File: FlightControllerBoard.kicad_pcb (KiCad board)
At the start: 2 copper layers, 50 x 60 mm, 88 parts, among them J1 Conn_01x02, J10 Conn_01x03_Male, J11 USB_C_Receptacle_USB2.0, J12 Conn_02x03_Odd_Even, J2 Conn_01x03_Male, J3 Conn_01x03_Male, J4 Conn_01x03_Male, J5 Conn_01x03_Male, J6 Conn_01x03_Male, J7 Conn_01x03_Male, J8 Conn_01x03_Male, J9 Conn_01x03_Male, Q1 BSS138, SW1 SW_Push, U1 FT230XQ, U2 LMZM23600, U3 ATmega2560-16AU, U4 BNO055, Y1 16MHz, Y2 32.768kHz

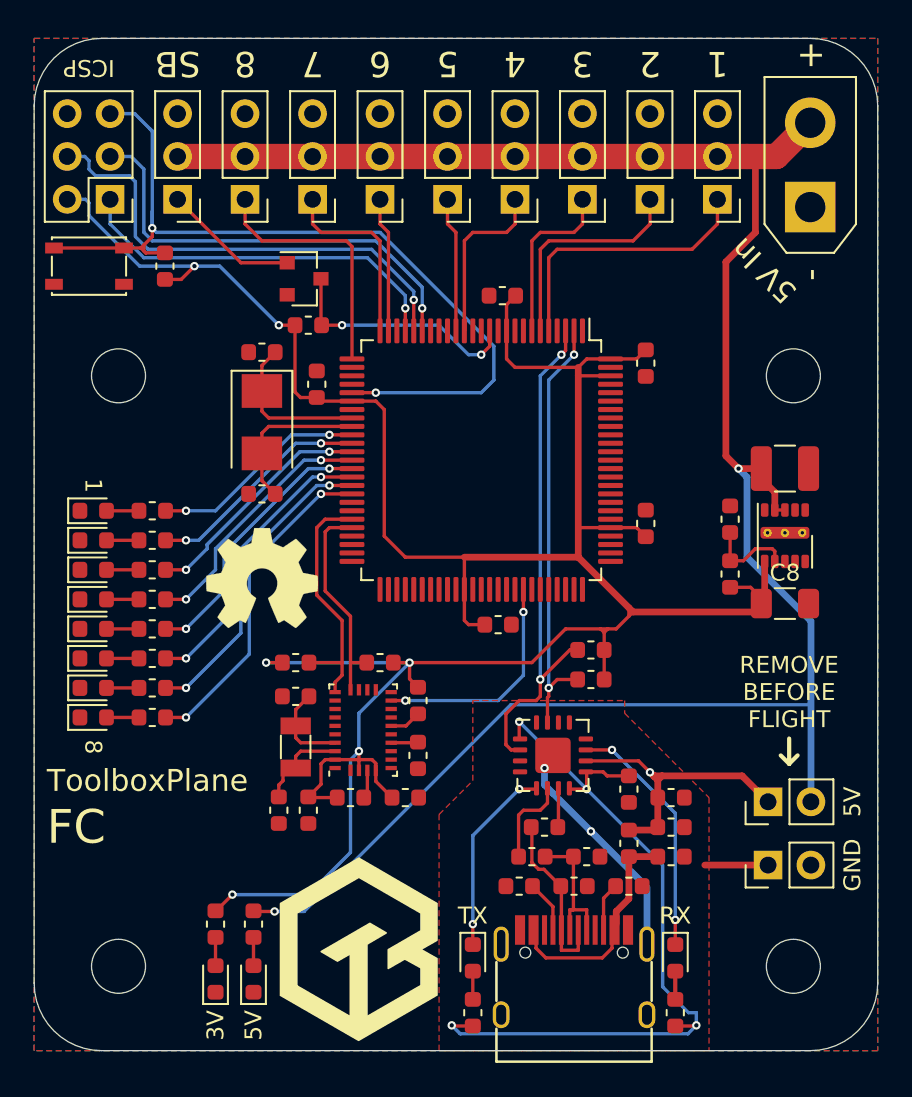
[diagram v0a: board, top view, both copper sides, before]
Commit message: optimize gnd connections
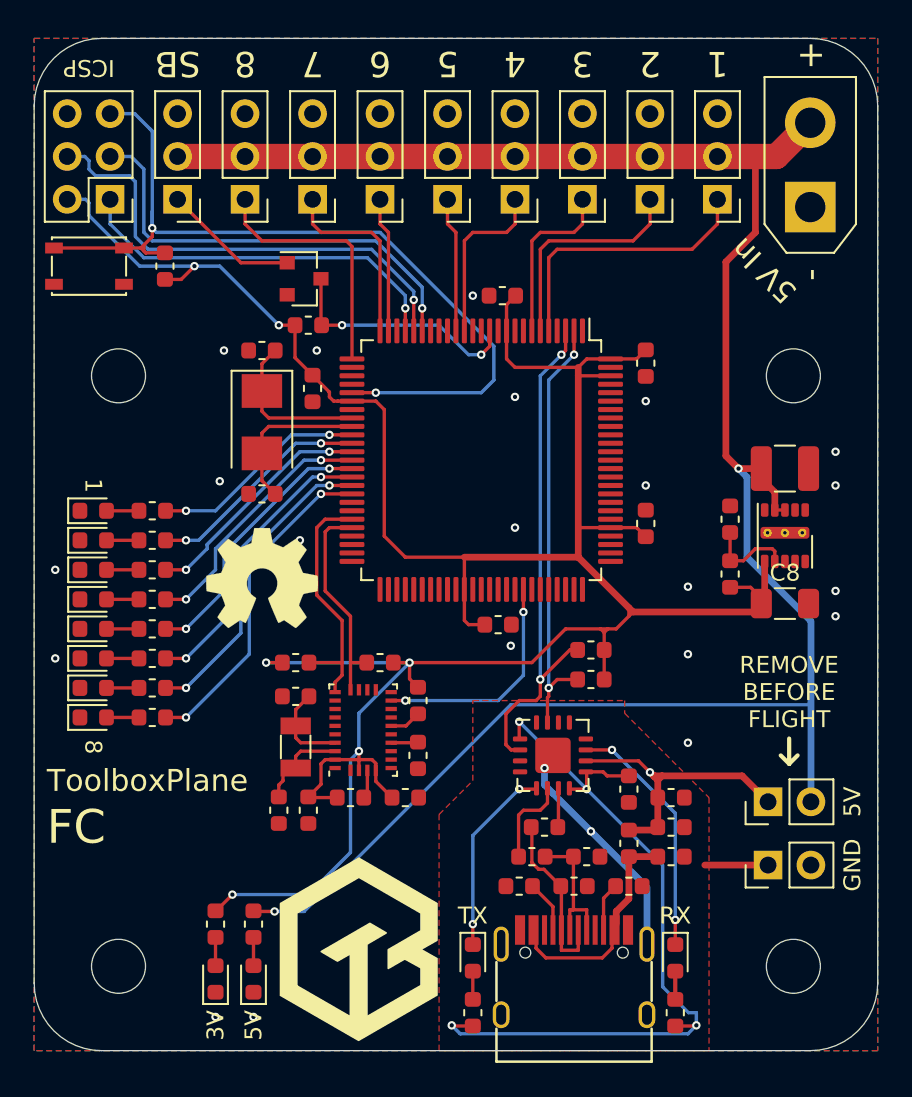
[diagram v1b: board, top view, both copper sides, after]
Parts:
- moved C12 0.35 mm to (16.5, 20.8), turned to 90 degrees
- moved C10 0.10 mm to (13.5, 18.5)
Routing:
- net +3V3: track 164.7 -> 163.7 mm
- net GND: vias 0 -> 21
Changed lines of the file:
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@@
     (thickness 1.6)
     (drawings 39)
-    (tracks 488)
+    (tracks 512)
     (zones 0)
     (modules 88)
@@
   )
   (module Capacitor_SMD:C_0603_1608Metric (layer F.Cu)
-    (at 16.75 20.5 270)
+    (at 16.5 20.75 90)
     (descr "Capacitor SMD 0603 (1608 Metric), square (rectangular) end terminal, IPC_7351 nominal, (Body size source: http://www.tortai-tech.com/upload/download/2011102023233369053.pdf), generated with kicad-footprint-generator")
     (tags capacitor)
     (attr smd)
-    (fp_text reference C12 (at 0 -1.43 270) (layer F.SilkS) hide
+    (fp_text reference C12 (at 0 -1.43 90) (layer F.SilkS) hide
       (effects (font (size 1 1) (thickness 0.15)))
     )
-    (fp_text value 100nF (at 0 1.43 270) (layer F.Fab)
+    (fp_text value 100nF (at 0 1.43 90) (layer F.Fab)
       (effects (font (size 1 1) (thickness 0.15)))
     )
-    (fp_text user %R (at 0 0 270) (layer F.Fab)
+    (fp_text user %R (at 0 0 90) (layer F.Fab)
       (effects (font (size 0.4 0.4) (thickness 0.06)))
     )
@@
     (fp_line (start -0.8 -0.4) (end 0.8 -0.4) (layer F.Fab) (width 0.1))
     (fp_line (start -0.8 0.4) (end -0.8 -0.4) (layer F.Fab) (width 0.1))
-    (pad 2 smd roundrect (at 0.7875 0 270) (size 0.875 0.95) (layers F.Cu F.Paste F.Mask) (roundrect_rratio 0.25)
+    (pad 2 smd roundrect (at 0.7875 0 90) (size 0.875 0.95) (layers F.Cu F.Paste F.Mask) (roundrect_rratio 0.25)
       (net 2 +3V3))
-    (pad 1 smd roundrect (at -0.7875 0 270) (size 0.875 0.95) (layers F.Cu F.Paste F.Mask) (roundrect_rratio 0.25)
+    (pad 1 smd roundrect (at -0.7875 0 90) (size 0.875 0.95) (layers F.Cu F.Paste F.Mask) (roundrect_rratio 0.25)
       (net 1 GND))
     (model ${KISYS3DMOD}/Capacitor_SMD.3dshapes/C_0603_1608Metric.wrl
@@
   )
   (module Capacitor_SMD:C_0603_1608Metric (layer F.Cu)
-    (at 13.5 18.6 180)
+    (at 13.5 18.5 180)
     (descr "Capacitor SMD 0603 (1608 Metric), square (rectangular) end terminal, IPC_7351 nominal, (Body size source: http://www.tortai-tech.com/upload/download/2011102023233369053.pdf), generated with kicad-footprint-generator")
     (tags capacitor)
@@
     (effects (font (size 1 1) (thickness 0.15)))
   )
+  (via (at 26 15.25) (size 0.5) (drill 0.25) (layers F.Cu B.Cu) (net 1))
+  (via (at 16.75 18.5) (size 0.5) (drill 0.25) (layers F.Cu B.Cu) (net 1))
+  (via (at 36.25 21.5) (size 0.5) (drill 0.25) (layers F.Cu B.Cu) (net 1))
+  (via (at 28.25 36) (size 0.5) (drill 0.25) (layers F.Cu B.Cu) (net 1))
+  (via (at 11.25 18.5) (size 0.5) (drill 0.25) (layers F.Cu B.Cu) (net 1))
+  (via (at 11 26.25) (size 0.5) (drill 0.25) (layers F.Cu B.Cu) (net 1))
+  (via (at 15.75 29.75) (size 0.5) (drill 0.25) (layers F.Cu B.Cu) (net 1))
+  (via (at 28.5 21.25) (size 0.5) (drill 0.25) (layers F.Cu B.Cu) (net 1))
+  (via (at 28.5 29) (size 0.5) (drill 0.25) (layers F.Cu B.Cu) (net 1))
+  (via (at 38.75 32.5) (size 0.5) (drill 0.25) (layers F.Cu B.Cu) (net 1))
+  (via (at 38.75 36.5) (size 0.5) (drill 0.25) (layers F.Cu B.Cu) (net 1))
+  (via (at 47.5 32.75) (size 0.5) (drill 0.25) (layers F.Cu B.Cu) (net 1))
+  (via (at 47.5 34.25) (size 0.5) (drill 0.25) (layers F.Cu B.Cu) (net 1))
+  (via (at 47.5 26.5) (size 0.5) (drill 0.25) (layers F.Cu B.Cu) (net 1))
+  (via (at 47.5 24.5) (size 0.5) (drill 0.25) (layers F.Cu B.Cu) (net 1))
+  (via (at 38.75 41.75) (size 0.5) (drill 0.25) (layers F.Cu B.Cu) (net 1))
+  (via (at 36.25 26.5) (size 0.5) (drill 0.25) (layers F.Cu B.Cu) (net 1))
+  (via (at 10.75 58) (size 0.5) (drill 0.25) (layers F.Cu B.Cu) (net 1))
+  (via (at 13 58) (size 0.5) (drill 0.25) (layers F.Cu B.Cu) (net 1))
+  (via (at 1.25 36.75) (size 0.5) (drill 0.25) (layers F.Cu B.Cu) (net 1))
+  (via (at 1.25 31.5) (size 0.5) (drill 0.25) (layers F.Cu B.Cu) (net 1))
   (segment (start 35.7125 29) (end 36.25 29.5375) (width 0.2) (layer F.Cu) (net 2) (status 20))
   (segment (start 34.1625 29) (end 35.7125 29) (width 0.2) (layer F.Cu) (net 2) (status 10))
@@
   (segment (start 25.75 34.75) (end 26.7125 34.75) (width 0.2) (layer F.Cu) (net 2) (status 20))
   (segment (start 25.5 34.5) (end 25.75 34.75) (width 0.2) (layer F.Cu) (net 2))
-  (segment (start 16.9625 21.5) (end 16.75 21.2875) (width 0.2) (layer F.Cu) (net 2) (status 30))
-  (segment (start 18.8375 21.5) (end 16.9625 21.5) (width 0.2) (layer F.Cu) (net 2) (status 30))
   (segment (start 43.3 33.3) (end 43.1 33.5) (width 0.4) (layer F.Cu) (net 2) (status 30))
   (segment (start 43.3 31.005) (end 43.3 33.3) (width 0.4) (layer F.Cu) (net 2) (status 30))
@@
   (segment (start 11 13.5) (end 14.5 17) (width 0.2) (layer B.Cu) (net 2))
   (segment (start 14.5 17) (end 15.4625 17) (width 0.2) (layer F.Cu) (net 2) (status 20))
-  (segment (start 15.4625 17) (end 15.4625 20.9625) (width 0.2) (layer F.Cu) (net 2) (status 10))
-  (segment (start 15.7875 21.2875) (end 16.75 21.2875) (width 0.2) (layer F.Cu) (net 2) (status 20))
-  (segment (start 15.4625 20.9625) (end 15.7875 21.2875) (width 0.2) (layer F.Cu) (net 2))
   (segment (start 3.04 9.54) (end 1.96 9.54) (width 0.2) (layer B.Cu) (net 2) (status 20))
   (segment (start 6.25 13.5) (end 3.25 10.5) (width 0.2) (layer B.Cu) (net 2))
@@
   (segment (start 10.7875 51.7125) (end 11.75 50.75) (width 0.2) (layer F.Cu) (net 2))
   (segment (start 10.75 51.7125) (end 10.7875 51.7125) (width 0.2) (layer F.Cu) (net 2))
+  (segment (start 18 21.5) (end 17.75 21.5) (width 0.2) (layer F.Cu) (net 2))
+  (segment (start 18.8375 21.5) (end 18 21.5) (width 0.2) (layer F.Cu) (net 2))
+  (segment (start 17.75 21.5) (end 17.5 21.25) (width 0.2) (layer F.Cu) (net 2))
+  (segment (start 17.5 21.25) (end 17.5 21) (width 0.2) (layer F.Cu) (net 2))
+  (segment (start 17.5 20.9625) (end 17.5 21) (width 0.2) (layer F.Cu) (net 2))
+  (segment (start 16.5 19.9625) (end 17.5 20.9625) (width 0.2) (layer F.Cu) (net 2))
+  (segment (start 15.4625 18.925) (end 16.5 19.9625) (width 0.2) (layer F.Cu) (net 2))
+  (segment (start 15.4625 17) (end 15.4625 18.925) (width 0.2) (layer F.Cu) (net 2))
   (segment (start 29.75 53.925) (end 29.75 52.85) (width 0.2) (layer F.Cu) (net 3) (status 20))
   (segment (start 30.325 54.5) (end 29.75 53.925) (width 0.2) (layer F.Cu) (net 3))
@@
   (segment (start 37.25 49) (end 32.75 44.5) (width 0.2) (layer B.Cu) (net 50))
   (segment (start 37.25 56.209963) (end 37.25 49) (width 0.2) (layer B.Cu) (net 50))
-  (segment (start 13.5 19.3875) (end 14.2875 18.6) (width 0.2) (layer F.Cu) (net 51) (status 20))
-  (segment (start 13.5 20.9) (end 13.5 19.3875) (width 0.2) (layer F.Cu) (net 51) (status 10))
   (segment (start 13.5 22.1) (end 13.5 20.9) (width 0.2) (layer F.Cu) (net 51) (status 20))
   (segment (start 13.9 22.5) (end 13.5 22.1) (width 0.2) (layer F.Cu) (net 51))
   (segment (start 13.9 22.5) (end 18.8375 22.5) (width 0.2) (layer F.Cu) (net 51))
+  (segment (start 13.5 19.2875) (end 14.2875 18.5) (width 0.2) (layer F.Cu) (net 51))
+  (segment (start 13.5 20.9) (end 13.5 19.2875) (width 0.2) (layer F.Cu) (net 51))
   (segment (start 22.7125 41.75) (end 22.75 41.7125) (width 0.2) (layer F.Cu) (net 52) (status 30))
   (segment (start 21.1625 41.75) (end 22.7125 41.75) (width 0.2) (layer F.Cu) (net 52) (status 30))

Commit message: fix LED resistor values
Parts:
- R15, R16, R17, R18, R19, R20, R21, R22: value 270 -> 100
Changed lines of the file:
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@@
-(kicad_pcb (version 20171130) (host pcbnew 5.1.0-060a0da~80~ubuntu18.04.1)
+(kicad_pcb (version 20171130) (host pcbnew 5.1.1)
   (general
     (thickness 1.6)
@@
       (effects (font (size 1 1) (thickness 0.15)))
     )
-    (fp_text value 270 (at 0 1.43 180) (layer F.Fab)
+    (fp_text value 100 (at 0 1.43 180) (layer F.Fab)
       (effects (font (size 1 1) (thickness 0.15)))
     )
@@
       (effects (font (size 1 1) (thickness 0.15)))
     )
-    (fp_text value 270 (at 0 1.43 180) (layer F.Fab)
+    (fp_text value 100 (at 0 1.43 180) (layer F.Fab)
       (effects (font (size 1 1) (thickness 0.15)))
     )
@@
       (effects (font (size 1 1) (thickness 0.15)))
     )
-    (fp_text value 270 (at 0 1.43 180) (layer F.Fab)
+    (fp_text value 100 (at 0 1.43 180) (layer F.Fab)
       (effects (font (size 1 1) (thickness 0.15)))
     )
@@
       (effects (font (size 1 1) (thickness 0.15)))
     )
-    (fp_text value 270 (at 0 1.43 180) (layer F.Fab)
+    (fp_text value 100 (at 0 1.43 180) (layer F.Fab)
       (effects (font (size 1 1) (thickness 0.15)))
     )
@@
       (effects (font (size 1 1) (thickness 0.15)))
     )
-    (fp_text value 270 (at 0 1.43 180) (layer F.Fab)
+    (fp_text value 100 (at 0 1.43 180) (layer F.Fab)
       (effects (font (size 1 1) (thickness 0.15)))
     )
@@
       (effects (font (size 1 1) (thickness 0.15)))
     )
-    (fp_text value 270 (at 0 1.43 180) (layer F.Fab)
+    (fp_text value 100 (at 0 1.43 180) (layer F.Fab)
       (effects (font (size 1 1) (thickness 0.15)))
     )
@@
       (effects (font (size 1 1) (thickness 0.15)))
     )
-    (fp_text value 270 (at 0 1.43 180) (layer F.Fab)
+    (fp_text value 100 (at 0 1.43 180) (layer F.Fab)
       (effects (font (size 1 1) (thickness 0.15)))
     )
@@
       (effects (font (size 1 1) (thickness 0.15)))
     )
-    (fp_text value 270 (at 0 1.43 180) (layer F.Fab)
-      (effects (font (size 1 1) (thickness 0.15)))
-    )
+    (fp_text value 100 (at 0 1.43 180) (layer F.Fab)
+      (effects (font (size 1 1) (thickness 0.15)))
+    )
